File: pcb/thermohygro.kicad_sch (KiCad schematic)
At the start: 5 parts, among them J1 RJ45_Shielded, J2 RJ45_Shielded, J3 SSD1306, U1 XIAO-ESP32-S3

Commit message: fixed fatal PCB failure which permanently destroys SHT85 if plugged. RJ45 pins were reversed and now placed in correct order.
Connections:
- net +3.3V: now also J1.6, J2.6; no longer J1.3, J2.3
- net GND: now also J1.3, J2.3; no longer J1.6, J2.6
- net SCK1: now also J1.5; no longer J1.4
- net SCK2: now also J2.5; no longer J2.4
- net SDA1: now also J1.4; no longer J1.5
- net SDA2: now also J2.4; no longer J2.5

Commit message: fixed 5V connected wrong instead of 3.3V. Now 3.3V
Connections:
- net +3.3V: now also U1.12 (3V3_OUT); no longer U1.14 (VBUS)
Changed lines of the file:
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@@
 	(title_block
 		(title "Thermohygro")
-		(date "2026-09-03")
-		(rev "1.1")
+		(date "2026-09-04")
+		(rev "1.2")
 	)
 	(junction
@@
 	(wire
 		(pts
-			(xy 154.94 118.11) (xy 154.94 121.92)
-		)
-		(stroke
-			(width 0)
-			(type default)
-		)
-	)
-	(wire
-		(pts
 			(xy 101.6 77.47) (xy 121.92 77.47)
 		)
@@
 		(pts
 			(xy 116.84 72.39) (xy 132.08 72.39)
-		)
-		(stroke
-			(width 0)
-			(type default)
-		)
-	)
-	(wire
-		(pts
-			(xy 151.13 118.11) (xy 151.13 121.92)
 		)
 		(stroke
@@
 	(symbol
 		(lib_id "power:+3.3V")
-		(at 154.94 121.92 180)
+		(at 147.32 118.11 180)
 		(unit 1)
 		(body_style 1)
@@
 		(in_pos_files yes)
 		(dnp no)
-		(fields_autoplaced yes)
 		(property "Reference" "#PWR04"
-			(at 154.94 118.11 0)
+			(at 147.32 114.3 0)
 			(hide yes)
 			(show_name no)
@@
 		)
 		(property "Value" "+3.3V"
-			(at 154.94 127 0)
+			(at 147.32 124.206 90)
 			(show_name no)
 			(do_not_autoplace no)
@@
 		)
 		(property "Footprint" ""
-			(at 154.94 121.92 0)
+			(at 147.32 118.11 0)
 			(hide yes)
 			(show_name no)
@@
 		)
 		(property "Datasheet" ""
-			(at 154.94 121.92 0)
+			(at 147.32 118.11 0)
 			(hide yes)
 			(show_name no)
@@
 		)
 		(property "Description" "Power symbol creates a global label with name \"+3.3V\""
-			(at 154.94 121.92 0)
+			(at 147.32 118.11 0)
 			(hide yes)
 			(show_name no)
@@
 	(symbol
 		(lib_id "power:GND")
-		(at 151.13 121.92 0)
+		(at 151.13 118.11 0)
 		(unit 1)
 		(body_style 1)
@@
 		(in_pos_files yes)
 		(dnp no)
-		(fields_autoplaced yes)
 		(property "Reference" "#PWR01"
-			(at 151.13 128.27 0)
+			(at 151.13 124.46 0)
 			(hide yes)
 			(show_name no)
@@
 		)
 		(property "Value" "GND"
-			(at 151.13 127 0)
+			(at 151.13 123.19 90)
 			(show_name no)
 			(do_not_autoplace no)
@@
 		)
 		(property "Footprint" ""
-			(at 151.13 121.92 0)
+			(at 151.13 118.11 0)
 			(hide yes)
 			(show_name no)
@@
 		)
 		(property "Datasheet" ""
-			(at 151.13 121.92 0)
+			(at 151.13 118.11 0)
 			(hide yes)
 			(show_name no)
@@
 		)
 		(property "Description" "Power symbol creates a global label with name \"GND\" , ground"
-			(at 151.13 121.92 0)
-			(hide yes)
-			(show_name no)
+			(at 151.13 118.11 0)
+			(hide yes)
+			(show_name no)

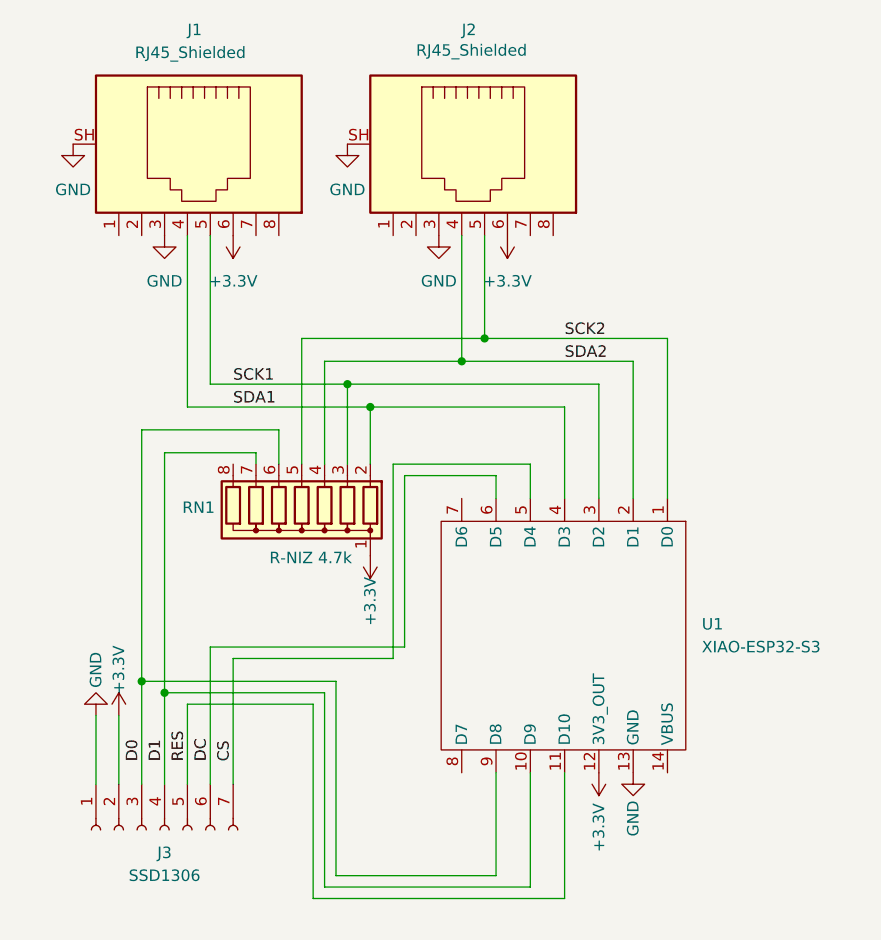
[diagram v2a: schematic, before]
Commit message: updated schematics with 8->10-pin R network, 7->8-pin display connector and additional wire to display
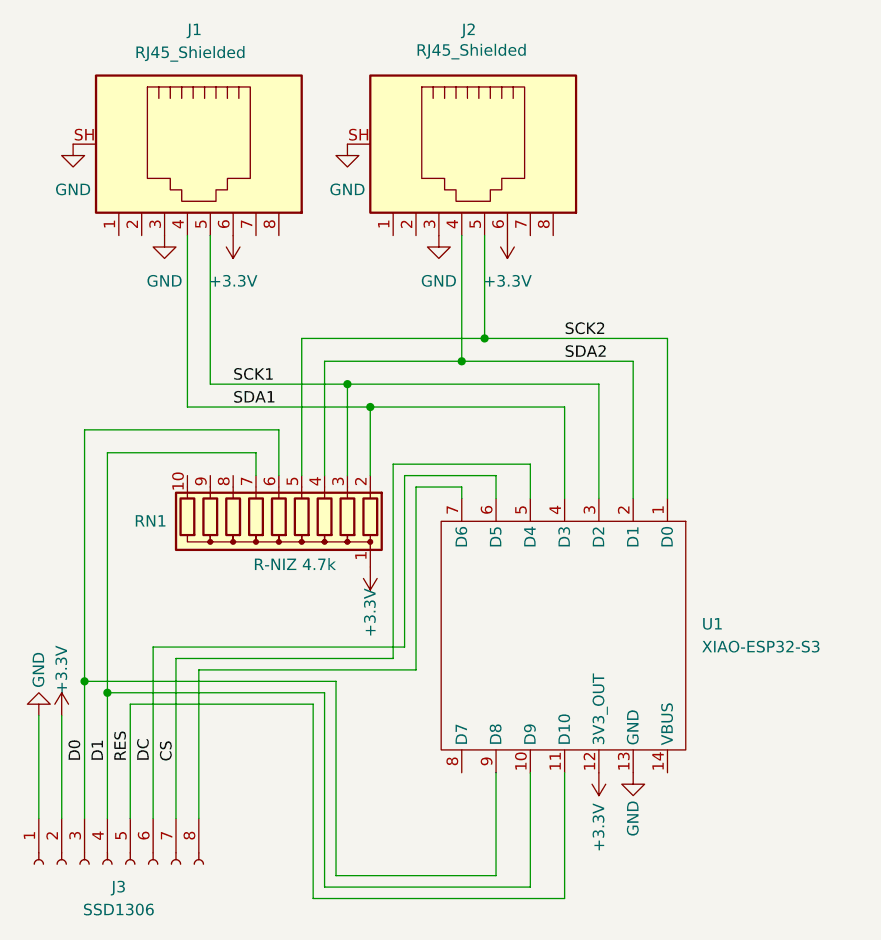
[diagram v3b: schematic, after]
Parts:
- removed J3: SSD1306, Connector_PinSocket_2.54mm:PinSocket_1x07_P2.54mm_Vertical, symbol Connector:Conn_01x07_Socket
- removed RN1: R-NIZ 4.7k, Resistor_THT:R_Array_SIP8, symbol Device:R_Network07
- added J3: SSD1306, Connector_PinSocket_2.54mm:PinSocket_1x08_P2.54mm_Vertical, symbol Connector:Conn_01x08_Socket
- added RN1: R-NIZ 4.7k, Resistor_THT:R_Array_SIP10, symbol Device:R_Network09
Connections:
- net +3.3V: now also J3.2 (Pin_2), RN1.1 (common)
- net CS: now also J3.7 (Pin_7)
- net D0: now also J3.3 (Pin_3), RN1.6 (R5)
- net D1: now also J3.4 (Pin_4), RN1.7 (R6)
- net DC: now also J3.6 (Pin_6)
- net GND: now also J3.1 (Pin_1)
- net RES: now also J3.5 (Pin_5)
- net SCK1: now also RN1.3 (R2)
- net SCK2: now also RN1.5 (R4)
- net SDA1: now also RN1.2 (R1)
- net SDA2: now also RN1.4 (R3)
- net at U1.7 (D6): now also J3.8 (Pin_8)
